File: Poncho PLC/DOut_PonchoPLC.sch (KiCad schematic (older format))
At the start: 66 parts, among them J10 TB_1X3, J11 TB_1X3, J6 TB_1X2, J7 TB_1X2, J8 TB_1X3, J9 TB_1X3, K1 RELAY_C, K2 RELAY_C, K3 RELAY_C, K4 RELAY_C, Q1 FQT13N06L, Q2 FQT13N06L, Q3 FQT13N06L, Q4 FQT13N06L, Q5 2N7002, Q6 2N7002, Q7 2N7002, Q8 2N7002, U3 MCP1416, U4 MCP1416, U5 MCP1416, U6 MCP1416

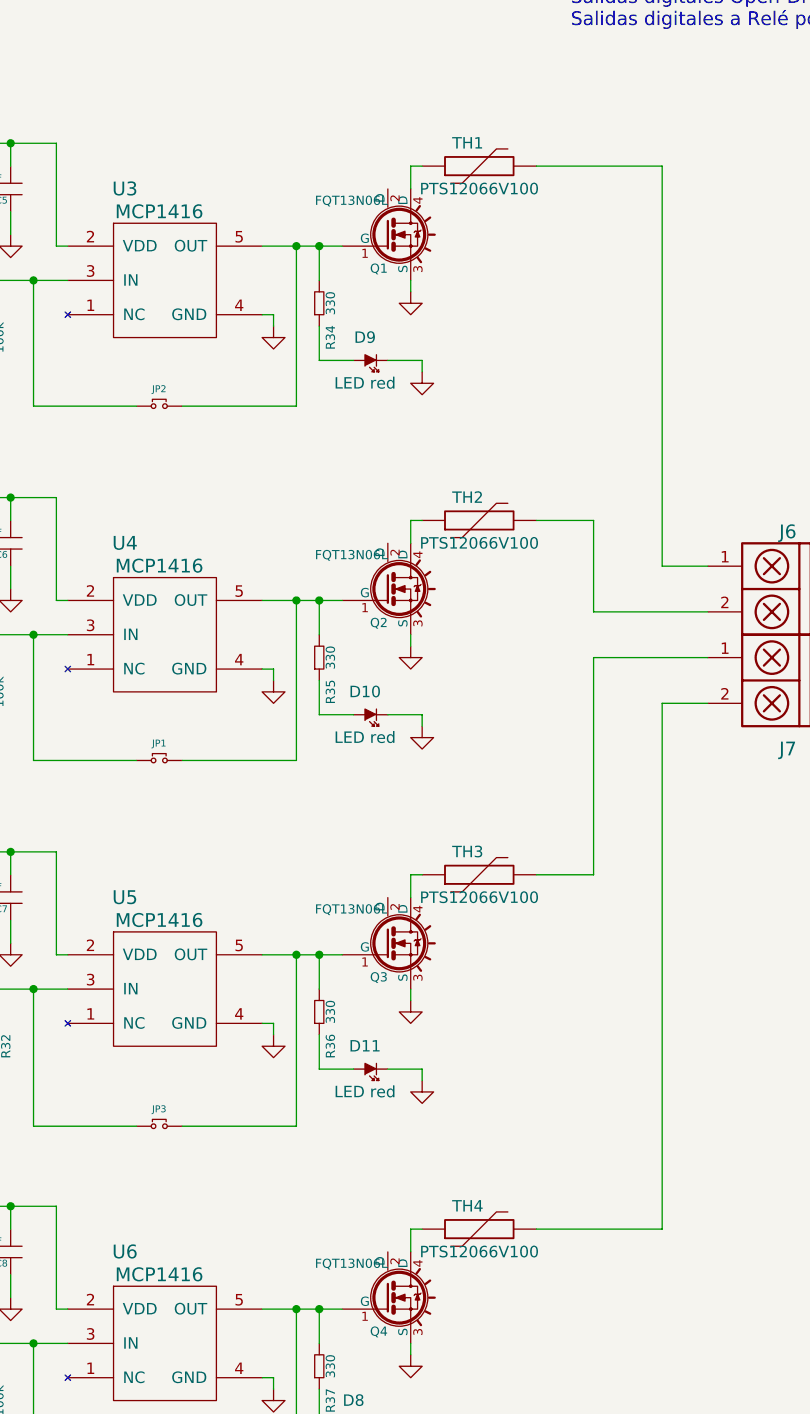
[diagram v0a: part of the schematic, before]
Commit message: Modifico visibilidad del pin del mosfet de salida.
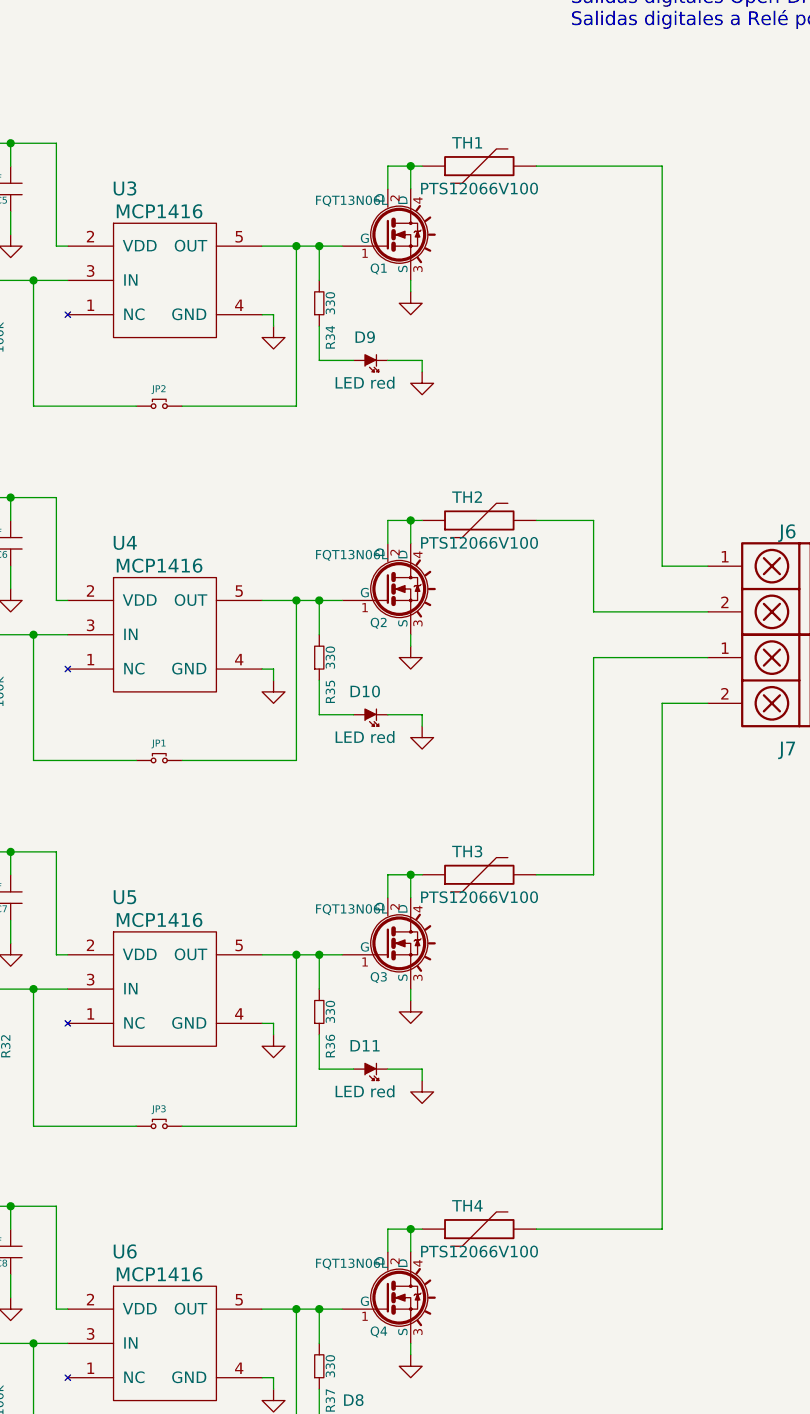
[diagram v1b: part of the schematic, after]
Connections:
- wire segments 212 -> 216
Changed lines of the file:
@@
 EESchema Schematic File Version 2
-LIBS:EESTN5
-LIBS:power
+LIBS:PonchoPLC
 LIBS:PonchoPLC-cache
 EELAYER 25 0
@@
 El circuito fue adaptado a componentes de proveedores locales.
 Wire Wire Line
-	3100 1550 3050 1550
-Wire Wire Line
-	3100 3100 3050 3100
-Wire Wire Line
-	3050 4650 3100 4650
-Wire Wire Line
-	3050 6200 3100 6200
+	2950 1550 3100 1550
+Wire Wire Line
+	2950 3100 3100 3100
+Wire Wire Line
+	2950 4650 3100 4650
+Wire Wire Line
+	2950 6200 3100 6200
 Wire Wire Line
 	1400 7250 1400 6700
@@
 	2550 7250 2550 6550
 Connection ~ 2550 6550
+Wire Wire Line
+	2950 6300 2950 6200
+Connection ~ 3050 6200
+Wire Wire Line
+	2950 4750 2950 4650
+Connection ~ 3050 4650
+Wire Wire Line
+	2950 3200 2950 3100
+Connection ~ 3050 3100
+Wire Wire Line
+	2950 1650 2950 1550
+Connection ~ 3050 1550
 $EndSCHEMATC

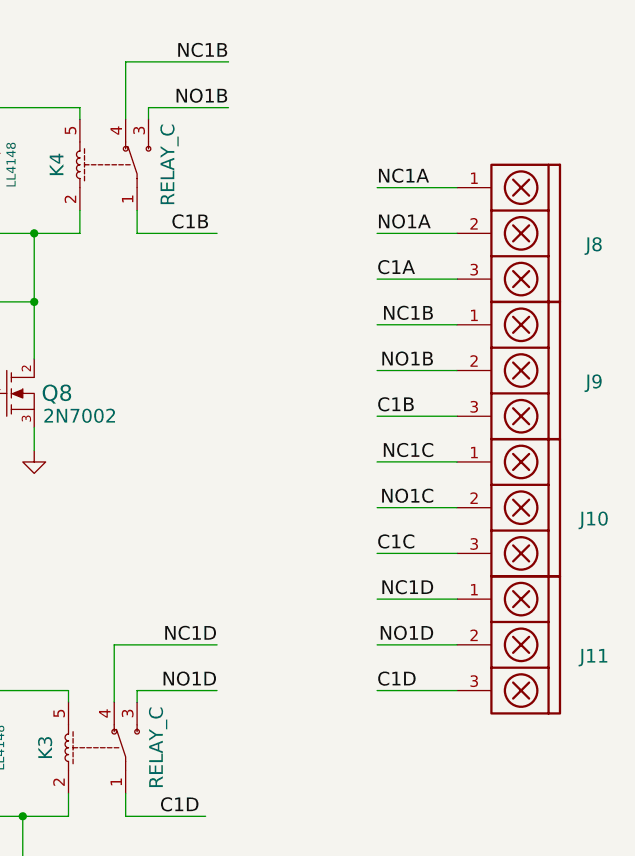
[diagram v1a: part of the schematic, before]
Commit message: Cambio SCH
Se modificaron algunas etiquetas para beneficiar el routeo del pcb en la
conexión Rele-Bornera.
Se actualizaron las referencias de las huellas de la librería anterior a
la actual, para lograr compatibilidad en el netlist y poder cargarlo al
pcb.
Se actualizaron los filtros de búsqueda de huellas en algunos
componentes de la librería de sch.
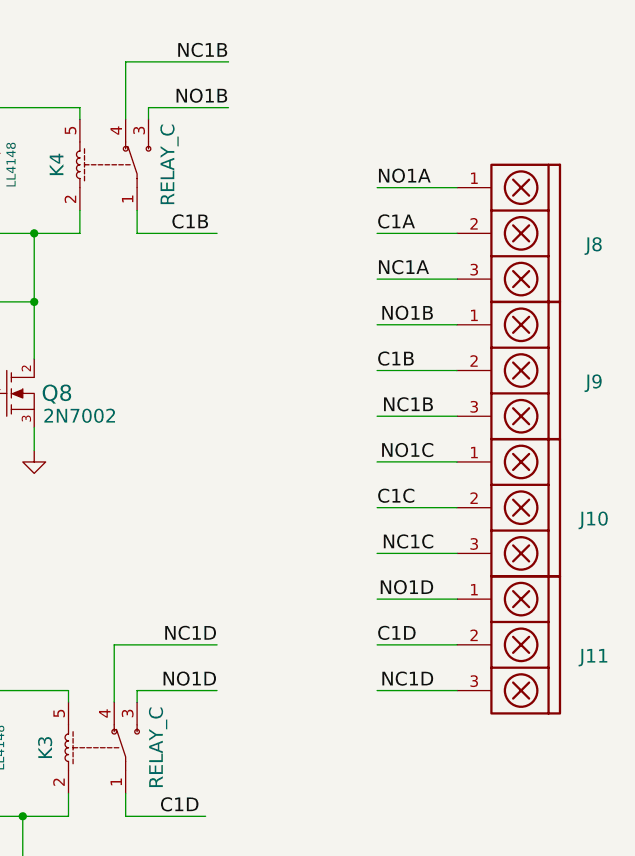
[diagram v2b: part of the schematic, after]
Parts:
- C1, C2, C3, C4, C5, C6, C7, C8: footprint EESTN5:C_1206 -> Poncho-PLC:C_1206
- D10, D11, D12, D13, D16, D17, D8, D9: footprint EESTN5:LED_1206 -> Poncho-PLC:LED_1206
- D14, D15, D18, D19: footprint EESTN5:SOD80C -> Poncho-PLC:SOD80C
- J10, J11, J8, J9: footprint EESTN5:BORNERA3 -> Poncho-PLC:BORNERA3
- J6, J7: footprint EESTN5:BORNERA3 -> Poncho-PLC:BORNERA2
- JP1, JP2, JP3, JP4: footprint EESTN5:Pin_strip_2 -> Poncho-PLC:Pin_strip_2
- K1, K2, K3, K4: footprint EESTN5:Relay_C -> Poncho-PLC:Relay_C
- Q1, Q2, Q3, Q4: footprint EESTN5:SOT-223 -> Poncho-PLC:SOT-223
- Q5, Q6, Q7, Q8: footprint EESTN5:SOT23 -> Poncho-PLC:SOT23
- R30, R31, R32, R33, R34, R35, R36, R37, R38, R39, R40, R41, R42, R43, R44, R45: footprint EESTN5:R_1206 -> Poncho-PLC:R_1206
- TH1, TH2, TH3, TH4: footprint EESTN5:PTC_1210 -> Poncho-PLC:PTC_1210
- U3, U4, U5, U6: footprint EESTN5:SOT-23-5 -> Poncho-PLC:SOT-23-5

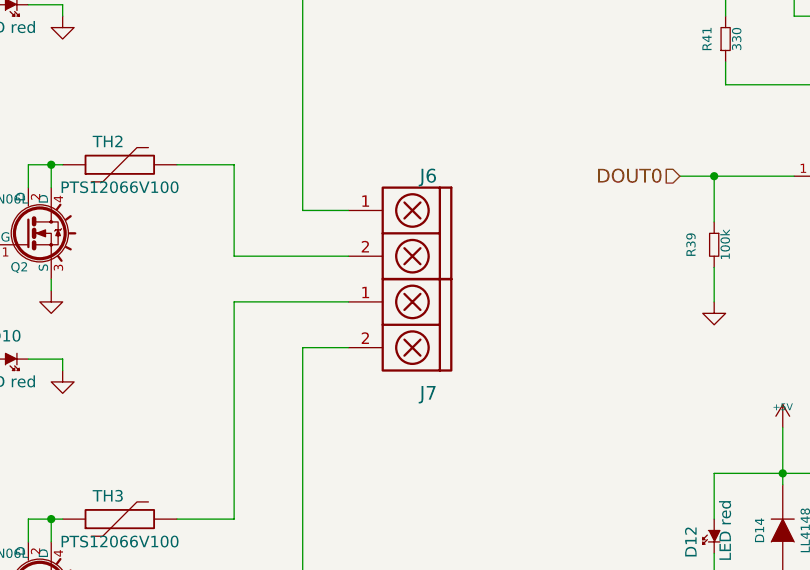
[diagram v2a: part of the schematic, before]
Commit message: Avance posicionamiento & Dimensión del poncho
Se avanzo en el posicionamiento de las entradas.
Se esta evaluando la dimensión del poncho y la posición de los agujeros
de sujeción.
A partir de ahora el diseño esta a cargo del Alumno Ignacio Vetrano
(E.E.S.T. N°5 - 5to 5ta)
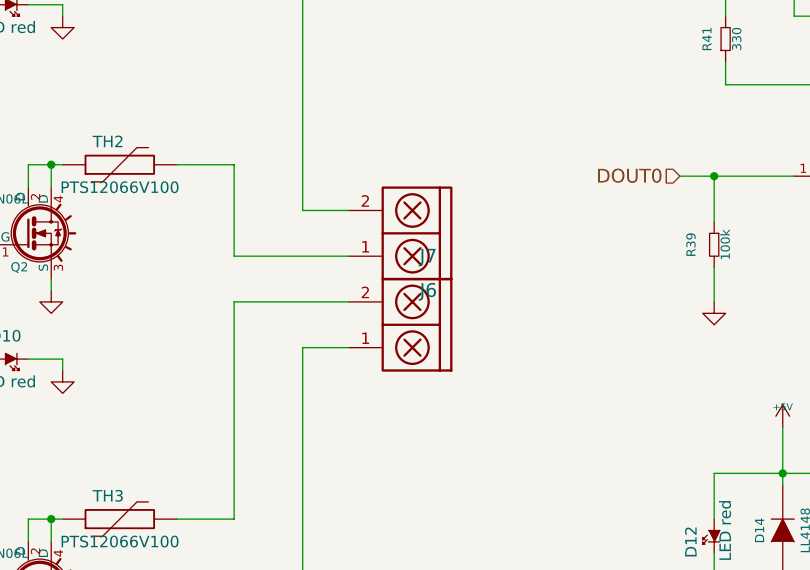
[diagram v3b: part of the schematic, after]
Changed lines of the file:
@@
 F 4 "Esqueleto EDU-CIAA" H 4700 3400 60  0001 C CNN "Title"
 	1    4700 3400
-	-1   0    0    -1
+	-1   0    0    1
 $EndComp
 $Comp
@@
 F 4 "Esqueleto EDU-CIAA" H 4700 3800 60  0001 C CNN "Title"
 	1    4700 3800
-	-1   0    0    -1
+	-1   0    0    1
 $EndComp
 Text Notes 1150 7450 0    60   ~ 0
